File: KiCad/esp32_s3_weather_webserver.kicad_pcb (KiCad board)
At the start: 4 copper layers, 132 parts, among them IC301 CP2102N-A02-GQFN28R, IC401 ESP32-S3-WROOM-1-N16R8, IC501 VEML7700-TT, IC502 DS3231MZ+TRL, J201 Barrel_Jack_Switch_Pin3Ring, J301 USB_C_Receptacle_USB2.0, J302 USB_C_Receptacle_USB2.0, J401 Conn_01x04_Pin, J402 Conn_01x04_Pin, J403 Conn_01x04_Pin, J404 TF-01A, J405 Conn_01x08_Pin, Q401 SS8050, Q402 SS8050, U201 AMS1117-3.3, U202 TLV62569DBV, U301 USBLC6-2SC6, U302 USBLC6-2SC6, U502 DS18B20, U503 LM35-LP, U504 DHT11

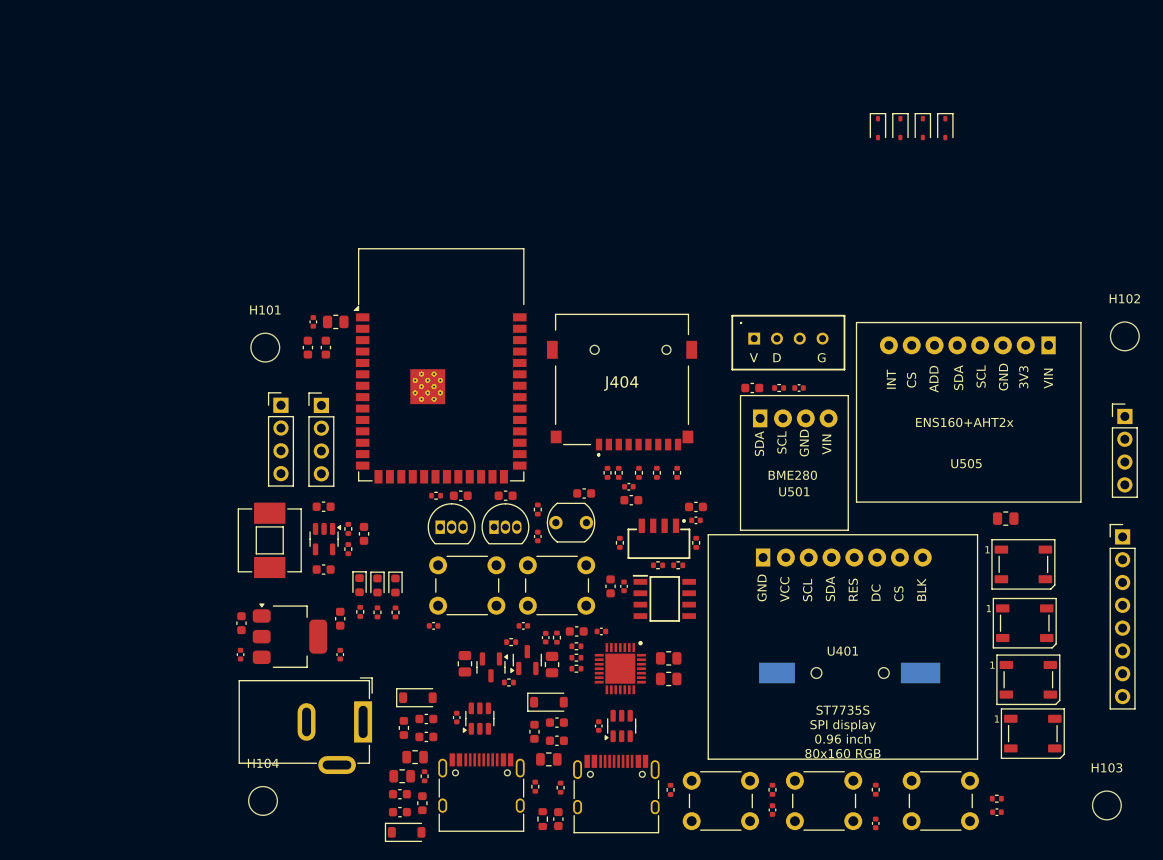
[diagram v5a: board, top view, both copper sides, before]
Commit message: PCB layout updates
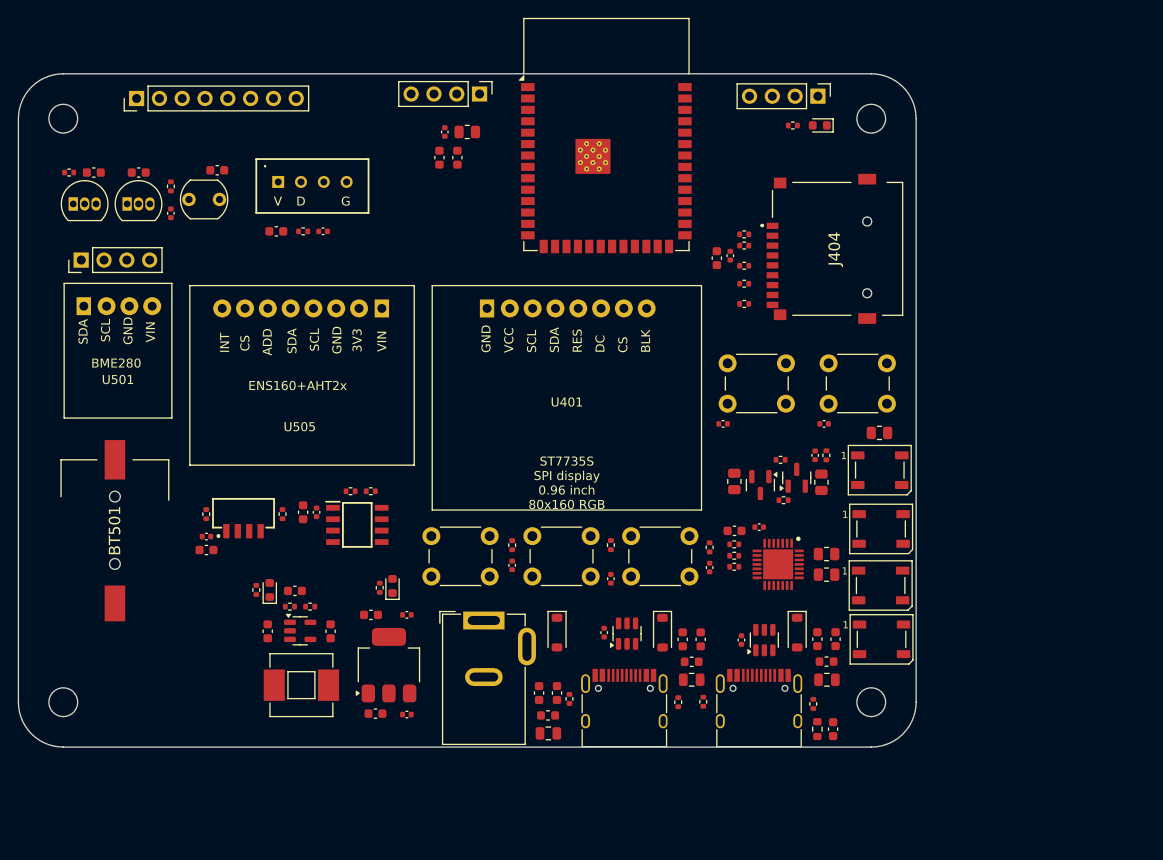
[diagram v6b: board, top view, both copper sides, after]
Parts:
- removed D401, D402, D403, D404: PESD3V3L1BA,115, Diode_SMD:D_SOD-323
- BT501: moved to F.Cu
- moved J405 120.2 mm to (38.2, 27.8), turned to 90 degrees
- moved J403 117.5 mm to (32.0, 45.8), turned to 90 degrees
- moved BT501 83.3 mm to (35.8, 76.0), turned to 90 degrees
- moved U501 76.4 mm to (30.1, 48.3)
- moved U505 74.4 mm to (44.1, 48.6)
- moved R206 70.0 mm to (111.3, 30.8), turned to 180 degrees
- moved D210 69.7 mm to (114.3, 30.8), turned to 180 degrees
- moved J402 69.0 mm to (114.1, 27.5), turned to -90 degrees
- moved C509 55.8 mm to (53.7, 42.5)
- moved C510 55.8 mm to (58.9, 42.5)
- moved R505 55.8 mm to (56.7, 42.5)
- moved U504 55.8 mm to (53.9, 37.0)
- moved C503 54.7 mm to (46.0, 78.0), turned to 0 degrees
- moved R502 54.7 mm to (45.9, 74.0), turned to 90 degrees
- moved C504 54.6 mm to (46.0, 76.5), turned to 0 degrees
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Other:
- board outline added: 100 x 75 mm

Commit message: PCB layout improvements
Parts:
- BT501: moved to B.Cu
- moved C503 49.9 mm to (63.0, 31.2), turned to 180 degrees
- moved C504 47.1 mm to (63.0, 32.7), turned to 180 degrees
- moved IC501 44.7 mm to (62.3, 33.7), turned to 180 degrees
- moved J405 44.3 mm to (31.0, 71.5), turned to 0 degrees
- moved R502 42.5 mm to (63.1, 35.2), turned to -90 degrees
- moved R503 38.9 mm to (54.6, 35.2), turned to -90 degrees
- moved BT501 37.8 mm to (71.8, 64.5), turned to 0 degrees
- moved J201 35.8 mm to (41.0, 86.0)
- moved D203 35.3 mm to (49.7, 88.6)
- moved R305 34.9 mm to (51.5, 94.3)
- moved C205 34.9 mm to (50.1, 93.6)
- moved C206 34.9 mm to (48.1, 93.6)
- moved FB201 34.9 mm to (49.1, 96.1)
- moved F201 34.9 mm to (49.1, 98.1)
- moved U501 34.5 mm to (38.1, 81.9), turned to 90 degrees
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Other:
- board size 100 x 75 mm -> 85 x 75 mm

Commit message: Simple routing
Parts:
- moved D201 32.8 mm to (49.0, 88.9)
- moved D203 32.1 mm to (81.8, 87.2)
- moved R305 20.0 mm to (71.5, 95.2)
- moved C204 10.3 mm to (65.5, 98.0)
- moved D210 10.1 mm to (105.8, 23.0)
- moved R206 10.1 mm to (102.8, 23.0)
- moved C203 9.27 mm to (65.5, 96.2), turned to 180 degrees
- moved D208 6.95 mm to (60.8, 85.7), turned to -90 degrees
- moved R204 4.00 mm to (62.2, 85.5), turned to 90 degrees
- moved C201 3.60 mm to (69.2, 98.0), turned to 0 degrees
- moved C302 2.87 mm to (89.8, 76.2), turned to 180 degrees
- moved U201 2.61 mm to (67.0, 90.8)
- moved C202 2.60 mm to (69.2, 96.2)
- moved BT501 2.26 mm to (69.5, 64.9)
- moved J403 2.15 mm to (33.5, 70.9)
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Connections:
- J401 pad 2: +3V3_PER -> +3V3
- J402 pad 2: +3V3_PER -> +3V3
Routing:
- net /[4] ESP32 S3/CHIP_PU: track 0.00 -> 97.7 mm, vias 0 -> 2
- net /[4] ESP32 S3/RXD0: track 0.00 -> 88.2 mm
- net USB_D-: track 0.00 -> 76.8 mm
- net USB_D+: track 0.00 -> 76.2 mm
- net /[4] ESP32 S3/TXD0: track 0.00 -> 74.6 mm
- net /[4] ESP32 S3/IO0_BTN: track 0.00 -> 35.7 mm
- net RTS: track 0.00 -> 20.8 mm
- net USB2UART_VBUS: track 0.00 -> 20.4 mm
- net USB_VBUS: track 0.00 -> 20.3 mm
- net FSPI_SS: track 0.00 -> 15.1 mm
- net /[3] USB/USB2UART_D-: track 0.00 -> 13.5 mm, vias 0 -> 2
- net /[3] USB/USB2UART_D+: track 0.00 -> 13.5 mm, vias 0 -> 2
- net DTR: track 0.00 -> 13.4 mm
- net /[3] USB/USB2UART_CONN_CC1: track 0.00 -> 8.07 mm
- net /[3] USB/USB_CONN_CC1: track 0.00 -> 7.76 mm
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- added copper zone on In1.Cu, net GND
- added copper zone on In2.Cu, net GND
